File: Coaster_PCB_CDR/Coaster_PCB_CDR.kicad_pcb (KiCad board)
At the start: 2 copper layers, 99.5 x 99 mm, 35 parts, among them J1 Vin, J10 GPIO_0-1, J11 5v, J12 5v, J13 GPIO_14-15, J14 5v, J15 GPIO_27-28, J16 5v, J17 5v, J18 5v, J2 Vin, J3 HC-05, J4 HC-05, J5 VCC_Batt, J6 3v3, J7 10V, J8 qwiic, J9 3v3, SW1 Vin_Switch, SW2 Vin_Switch, SW3 Vin_Switch, U1 PicoW, U2 LM2937xT

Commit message: final please
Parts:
- removed the H2 at (169.8, 149.8)
- removed the J18 at (65.0, 120.3)
- added J10: Conn_01x04, Connector_JST:JST_SH_SM04B-SRSS-TB_1x04-1MP_P1.00mm_Horizontal, F.Cu at (137.0, 67.0)
- SW1: value Vin_Switch -> sigma
- SW2: value Vin_Switch -> beta
- SW3: value Vin_Switch -> alpha
- moved J9 4.00 mm to (117.6, 65.6)
- moved J15 2.63 mm to (84.3, 121.4)
- renumbered H3 to H2, J10 to J12, J12 to J13, J13 to J15, J15 to J17, J17 to J18, J5 to J3, J3 to J4, J7 to J5, J4 to J6, J6 to J7, J9 to J8, J8 to J9
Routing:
- net GPIO16: track 101.8 -> 132.8 mm
- net GPIO1: track 54.8 -> 75.2 mm
- net GPIO0: track 51.2 -> 66.4 mm
- net GPIO14: track 28.8 -> 34.7 mm
- net GPIO15: track 29.8 -> 35.1 mm
- net +3V3: track 82.6 -> 87.6 mm
- net VSYS: track 248.3 -> 249.7 mm
- net GPIO17: track 135.2 -> 136.5 mm
- net RF1: track 35.8 -> 34.8 mm
- net RF2: track 36.4 -> 35.7 mm
- net GND: vias 110 -> 131

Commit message: final finalish
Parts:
- added C1: 2200uF, Capacitor_THT:CP_Radial_D10.0mm_P5.00mm, F.Cu at (167.7, 149.6)
- J17: renamed from J10; value Conn_01x04 -> qwiic
- renumbered C1 to C2, C2 to C3, J11 to J10, J12 to J11, J13 to J12, J14 to J13, J15 to J14, J16 to J15, J17 to J16, SW3 to SW2, SW2 to SW3

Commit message: some refinements
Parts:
- added J12: 5v, Connector_PinSocket_2.54mm:PinSocket_1x02_P2.54mm_Vertical, F.Cu at (84.4, 133.2)
- moved J9 2.47 mm to (117.7, 68.1)
- moved J18 1.48 mm to (136.8, 65.6)
- turned J10 to 90 degrees
- turned J13 to -90 degrees
- turned J7 to -90 degrees
- turned J8 to 90 degrees
- renumbered J12 to J13, J13 to J14, J14 to J15, J15 to J16, J16 to J17, J17 to J18, J18 to J19
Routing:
- net +3V3: track 87.6 -> 106.4 mm
- net VSYS: track 249.7 -> 266.7 mm
- net GPIO0: track 66.4 -> 76.4 mm
- net GPIO1: track 75.2 -> 77.4 mm
- net RF1: track 34.8 -> 35.9 mm
- net RF2: track 35.7 -> 36.7 mm
- net GND: vias 131 -> 137

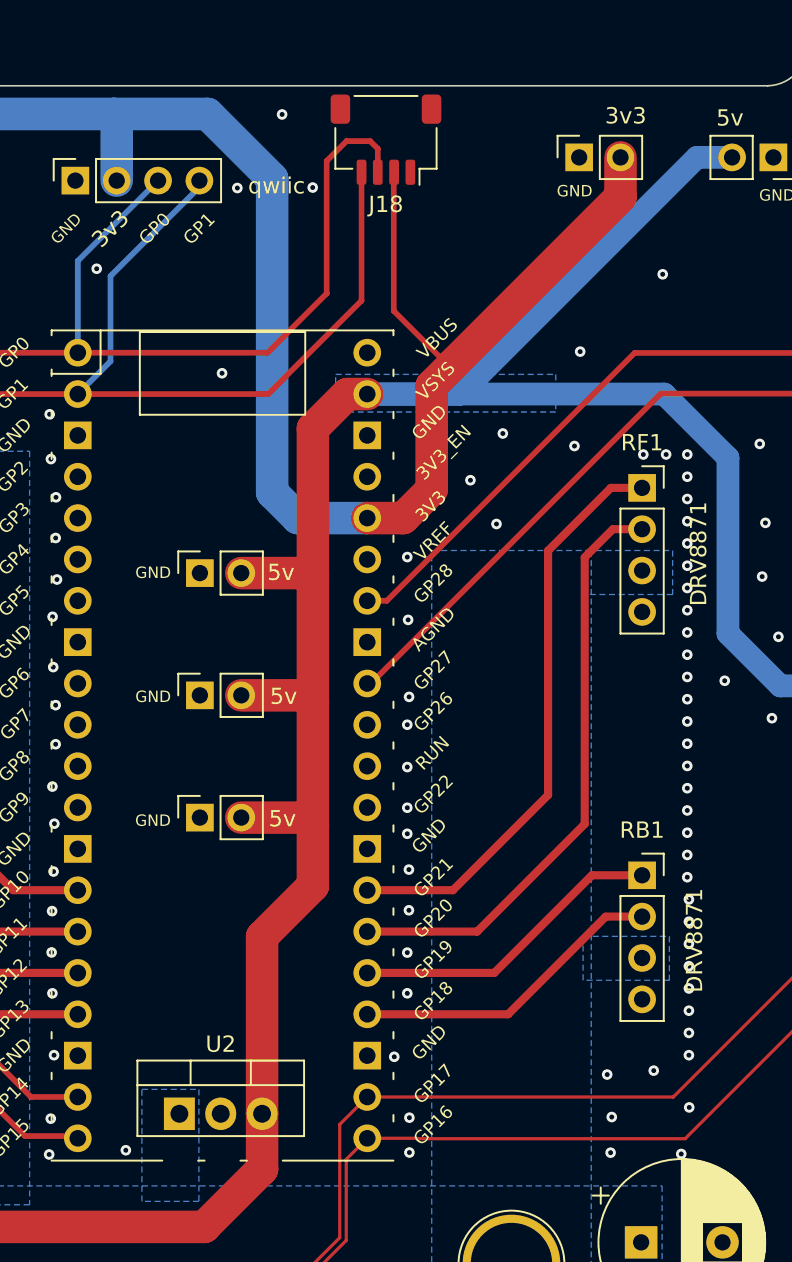
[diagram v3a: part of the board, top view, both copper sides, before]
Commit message: added vias
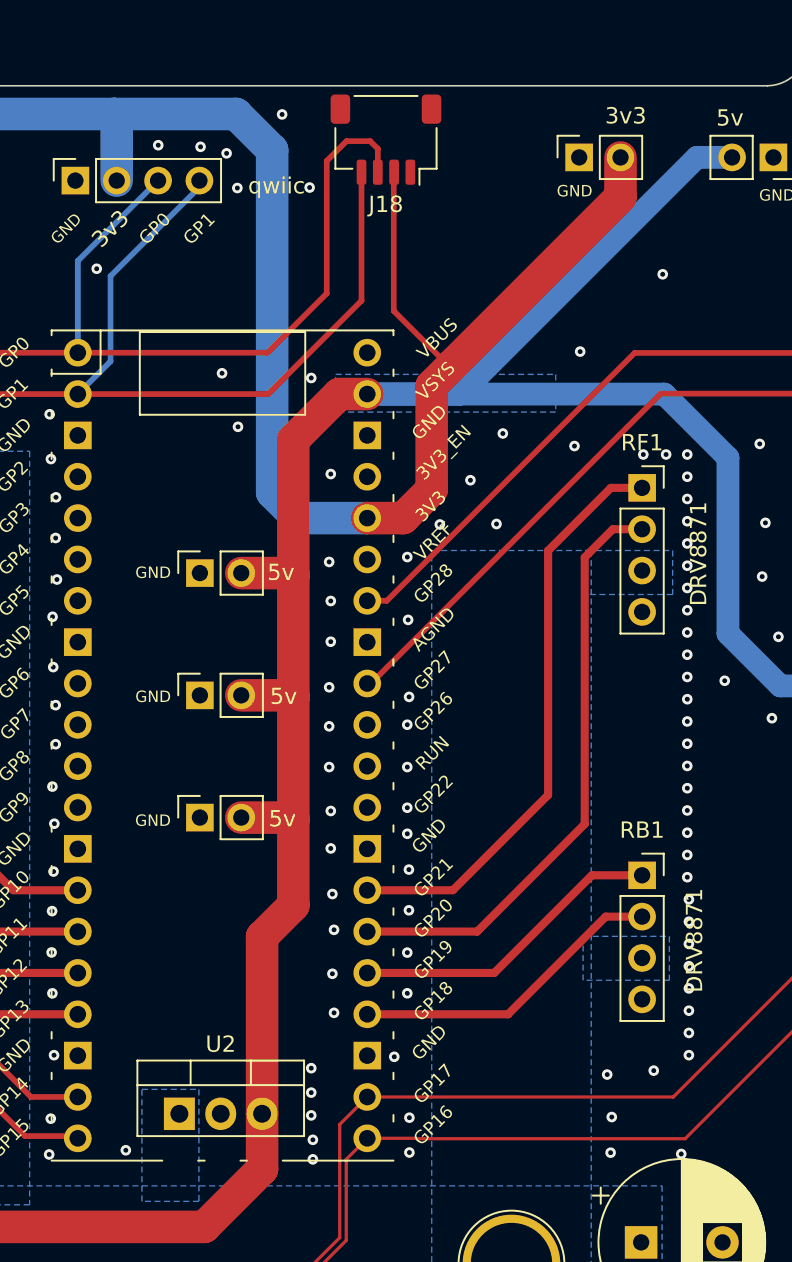
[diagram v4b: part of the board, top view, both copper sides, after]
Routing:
- net VSYS: track 266.7 -> 263.0 mm
- net +3V3: track 106.4 -> 107.4 mm
- net GND: vias 137 -> 160

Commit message: antooonie
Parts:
- removed J3: VCC_Batt, TestPoint:TestPoint_Plated_Hole_D5.0mm
- J5: footprint TestPoint:TestPoint_Plated_Hole_D5.0mm -> TestPoint:TestPoint_Plated_Hole_D3.0mm
- R1: value 330 -> 1k; footprint Resistor_THT:R_Axial_DIN0204_L3.6mm_D1.6mm_P7.62mm_Horizontal -> Resistor_THT:R_Axial_DIN0207_L6.3mm_D2.5mm_P10.16mm_Horizontal
- moved C1 5.44 mm to (162.3, 149.5)
- moved R1 3.67 mm to (165.7, 130.1)
- moved J1 2.51 mm to (88.3, 149.6)
- moved J2 2.47 mm to (90.8, 141.0)
- moved D2 0.70 mm to (165.6, 123.2)
- moved J4 0.30 mm to (84.3, 109.2)
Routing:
- net Net-(D2-Pad2): track 8.62 -> 4.40 mm
- net GPIO0: track 76.4 -> 77.0 mm
- net GND: vias 160 -> 161
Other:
- outline, holes or cut-outs redrawn

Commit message: removed edges
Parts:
- moved H2 7.39 mm to (165.8, 70.5)
- moved H1 7.34 mm to (87.6, 70.5)
- moved J10 1.98 mm to (92.2, 64.7)
- moved J8 1.98 mm to (148.8, 64.7)
- moved J7 1.93 mm to (103.2, 64.7)
- moved J13 1.93 mm to (160.7, 64.7)
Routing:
- net +3V3: track 107.4 -> 111.2 mm
- net VSYS: track 262.7 -> 265.2 mm
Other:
- board size 99.5 x 99 mm -> 89.5 x 94.2 mm

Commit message: done with fdr pcb?
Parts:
- removed the C1 at (162.3, 149.5)
- removed the J10 at (92.2, 64.7)
- removed J12, J14, J16, J19: 5v, Connector_PinSocket_2.54mm:PinSocket_1x02_P2.54mm_Vertical
- removed the J4 at (84.3, 109.2)
- removed the J6 at (168.7, 96.6)
- removed the J7 at (103.2, 64.7)
- removed the SW2 at (107.2, 142.6)
- removed SW3: beta, Buggy_Footprints:omar_3pin_switch
- added SW1: sigma, Buggy_Footprints:omar_3pin_switch, F.Cu at (119.5, 142.6)
- J2: value Vin -> HC-05; footprint Connector_PinSocket_2.54mm:PinSocket_1x02_P2.54mm_Vertical -> Connector_PinSocket_2.54mm:PinSocket_1x06_P2.54mm_Vertical
- moved J2 85.7 mm to (129.8, 64.6), turned to -90 degrees
- moved H1 33.8 mm to (98.5, 102.5)
- moved H2 33.4 mm to (155.5, 102.3)
- moved J4 14.9 mm to (159.1, 75.4), turned to 180 degrees
- moved J1 12.6 mm to (100.3, 145.9)
- moved D2 12.3 mm to (153.5, 125.3), turned to 0 degrees
- moved J5 11.8 mm to (106.4, 64.6), turned to -90 degrees
- moved J8 10.5 mm to (94.4, 124.4)
- moved J6 10.2 mm to (94.5, 78.7)
- moved J9 10.1 mm to (159.1, 82.0)
- moved R1 9.07 mm to (156.7, 131.2)
- moved C2 6.93 mm to (145.5, 133.3)
- moved J3 6.81 mm to (139.3, 139.0)
- moved J10 5.84 mm to (142.6, 66.1)
- moved J7 4.38 mm to (159.1, 68.8), turned to 180 degrees
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- renumbered C2 to C1, C3 to C2, J18 to J10, J5 to J3, J8 to J4, J9 to J5, J11 to J6, J13 to J7, J15 to J8, J17 to J9, SW1 to SW2
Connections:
- J10 pad 3: GPIO0 -> SDA
- J10 pad 4: GPIO1 -> SCL
- J2 pad 1: GND -> unconnected-(J2-Pad1)
- J2 pad 2: VCC -> VSYS
- J5 pad 3: GPIO0 -> SDA
- J5 pad 4: GPIO1 -> SCL
- U1 pad 21: GPIO16 -> unconnected-(U1-Pad21)
- U1 pad 22: GPIO17 -> unconnected-(U1-Pad22)
- U1 pad 6: GPIO4 -> SDA
- U1 pad 7: GPIO5 -> SCL
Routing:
- net VSYS: track 265.2 -> 97.7 mm, vias 1 -> 0
- net GPIO17: track 136.2 -> 0.00 mm
- net GPIO16: track 132.5 -> 0.00 mm
- net SCL: track 0.00 -> 74.4 mm, vias 0 -> 1
- net SDA: track 0.00 -> 68.9 mm
- net GPIO0: track 77.0 -> 38.1 mm
- net GPIO1: track 77.4 -> 41.7 mm
- net +3V3: track 111.2 -> 98.5 mm
- net GPIO15: track 35.1 -> 23.4 mm, vias 1 -> 0
- net GPIO14: track 34.7 -> 23.4 mm, vias 1 -> 0
- net GPIO28: track 39.9 -> 29.4 mm
- net GPIO27: track 40.9 -> 30.5 mm
- net RF2: track 36.7 -> 32.0 mm
- net RF1: track 35.9 -> 31.7 mm
- net Net-(D2-Pad2): track 4.40 -> 6.18 mm
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- removed copper zone on B.Cu, net VSYS
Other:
- board size 89.5 x 94.2 mm -> 69.5 x 94.2 mm
- board text added: "GP4"
- board text added: "GP5"
- board text removed: "GP16"
- board text removed: "GP17"

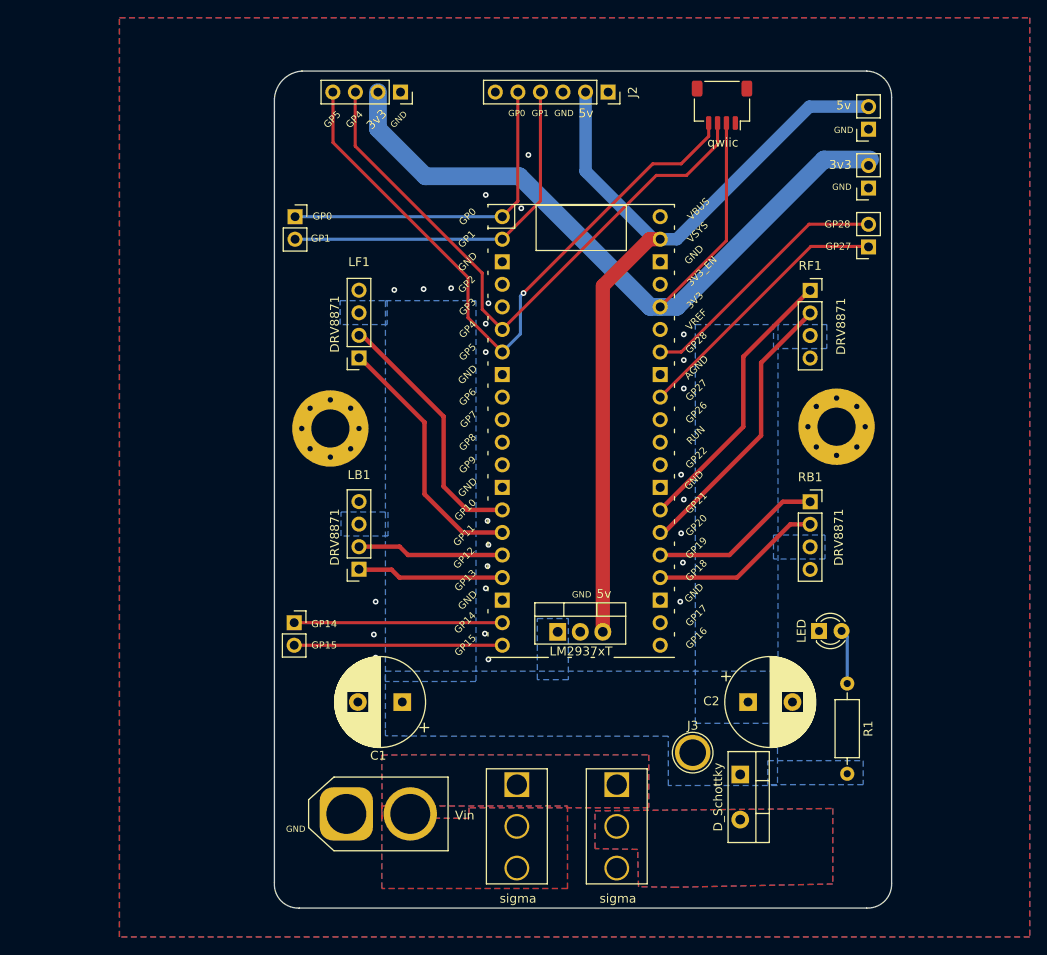
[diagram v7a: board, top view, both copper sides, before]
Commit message: fdr pcb minimized
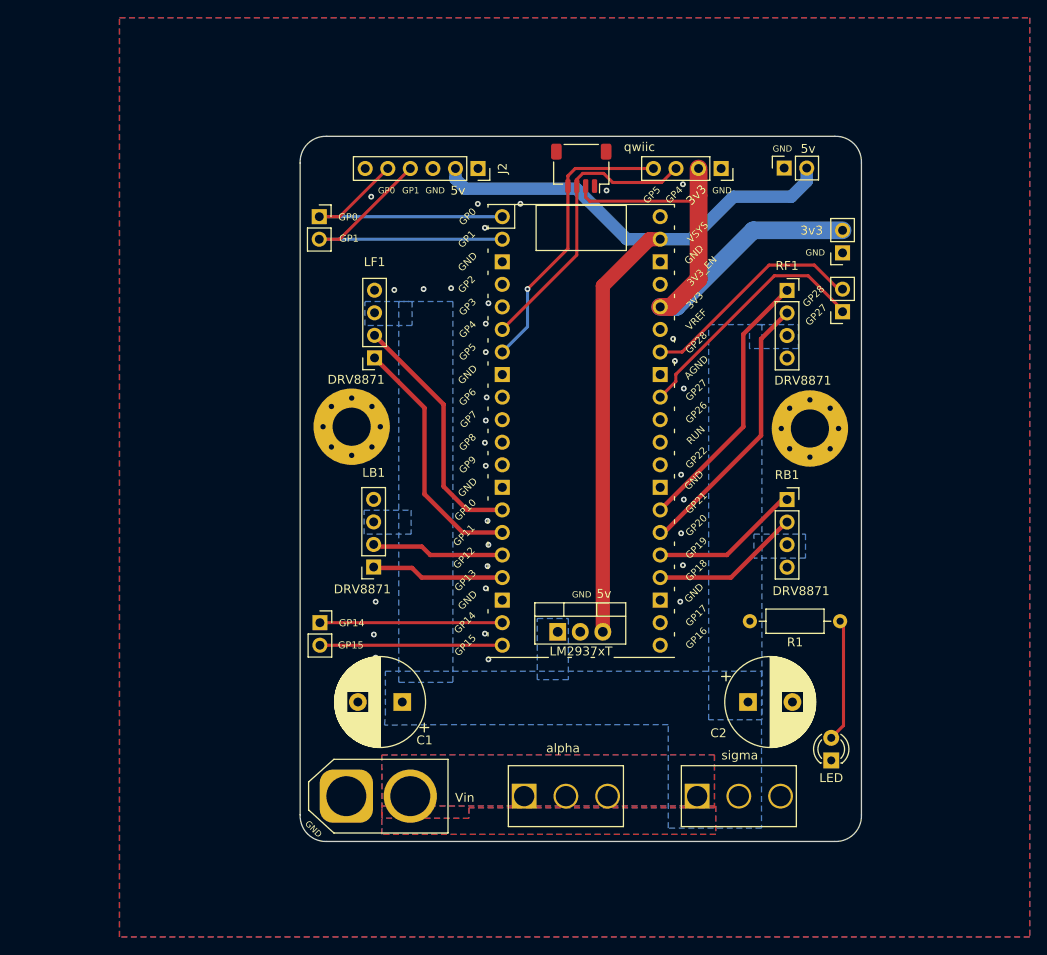
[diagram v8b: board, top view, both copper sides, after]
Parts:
- removed D1: D_Schottky, Package_TO_SOT_THT:TO-220-2_Vertical
- removed J3: 10V, TestPoint:TestPoint_Plated_Hole_D3.0mm
- SW1: value sigma -> alpha
- moved J5 37.1 mm to (142.5, 73.2)
- moved J10 17.4 mm to (126.8, 73.2)
- moved J2 17.0 mm to (115.1, 73.2)
- moved D2 14.6 mm to (154.9, 139.9), turned to 90 degrees
- moved J7 10.5 mm to (149.6, 73.2), turned to 90 degrees
- moved SW2 9.14 mm to (139.8, 143.9), turned to 90 degrees
- moved J4 7.86 mm to (156.2, 82.7)
- moved J9 7.86 mm to (156.2, 89.3)
- moved R1 7.07 mm to (155.9, 124.2), turned to 180 degrees
- moved H2 3.01 mm to (152.5, 102.5)
- moved J8 2.90 mm to (97.3, 124.4)
- moved J6 2.72 mm to (97.2, 78.7)
- moved RB1 2.61 mm to (149.9, 110.5)
- moved RF1 2.60 mm to (149.9, 87.0)
- moved H1 2.41 mm to (100.9, 102.3)
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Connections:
- SW2 pad 2: VCC_Batt -> vBatt
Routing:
- net SCL: track 74.4 -> 32.9 mm
- net +3V3: track 98.5 -> 58.1 mm
- net SDA: track 68.9 -> 32.9 mm
- net Net-(D2-Pad2): track 6.18 -> 13.7 mm
- net GPIO1: track 41.7 -> 34.2 mm
- net GPIO0: track 38.1 -> 30.6 mm
- net GPIO28: track 29.4 -> 25.7 mm
- net GPIO15: track 23.4 -> 20.5 mm
- net GPIO14: track 23.4 -> 20.5 mm
- net RB1: track 19.4 -> 16.9 mm
- net RB2: track 19.4 -> 16.9 mm
- net VSYS: track 97.7 -> 95.3 mm
- net GPIO27: track 30.5 -> 28.4 mm
- net LB2: track 16.5 -> 15.0 mm
- net LB1: track 16.3 -> 15.0 mm
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- removed copper zone on B.Cu, net VCC_Batt
- removed copper zone on F.Cu, net VCC_Batt
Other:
- board size 69.5 x 94.2 mm -> 63.2 x 79.4 mm
